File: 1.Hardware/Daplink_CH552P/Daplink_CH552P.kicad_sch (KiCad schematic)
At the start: 19 parts, among them J1 Conn_02x05_Counter_Clockwise, J2 USB_C_Receptacle_USB2.0, SW1 SW_Push, U1 SN74LVC1T45DBV, U2 SN74LVC1T45DBV, U3 CH552G, U4 XC6206P332MR

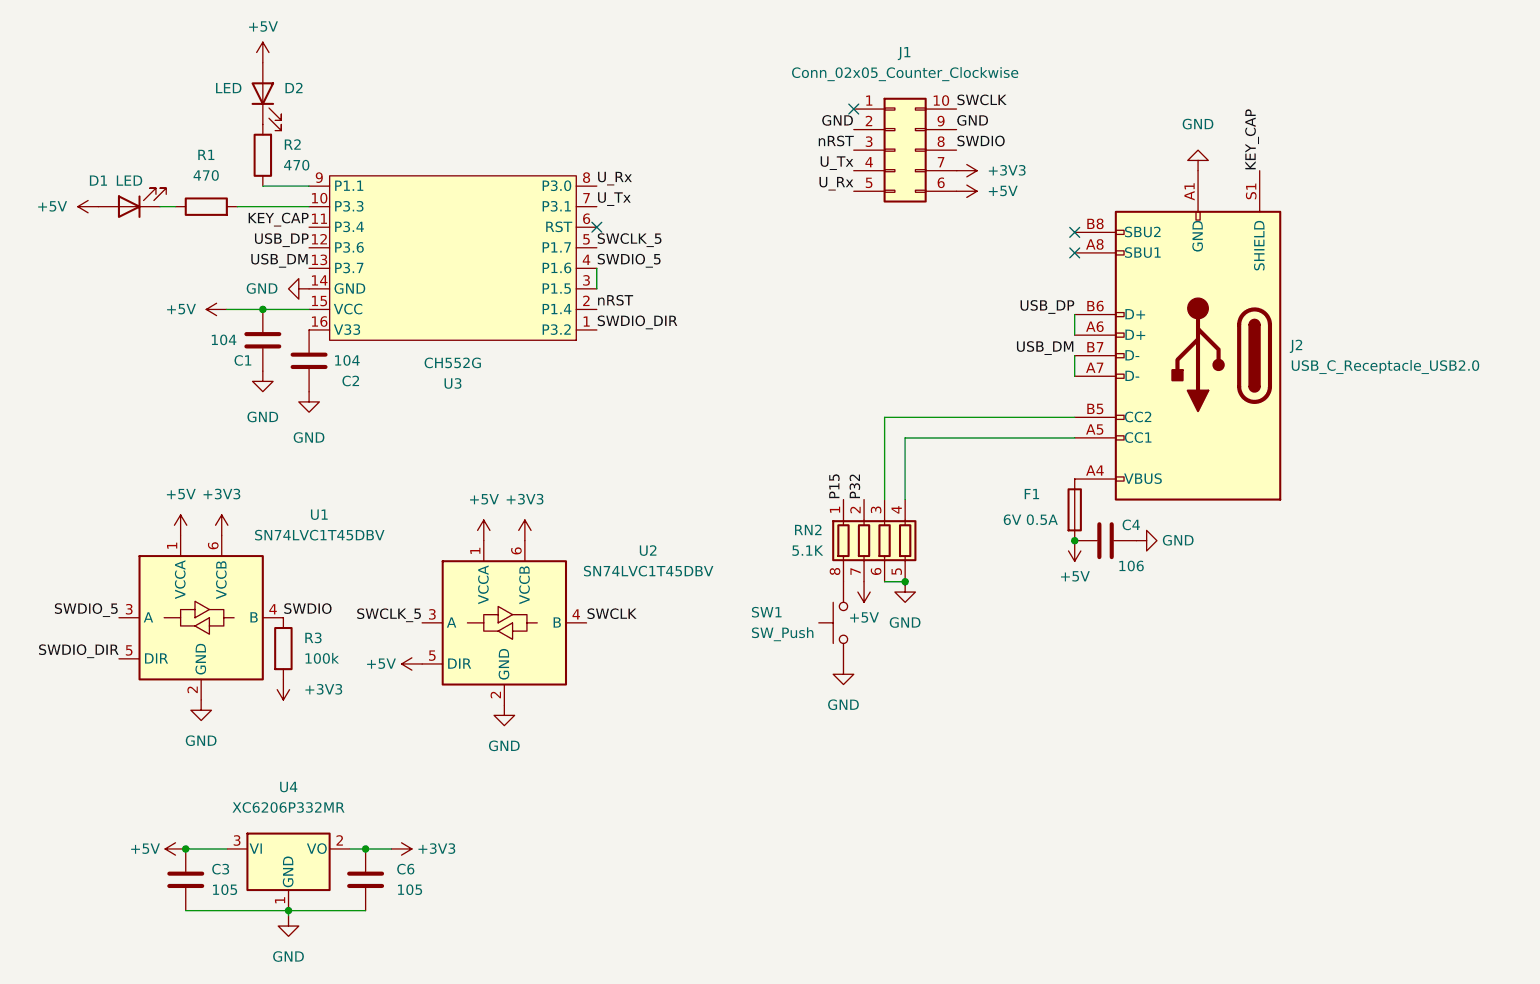
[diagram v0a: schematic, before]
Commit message: 更新调试器硬件（未测试）
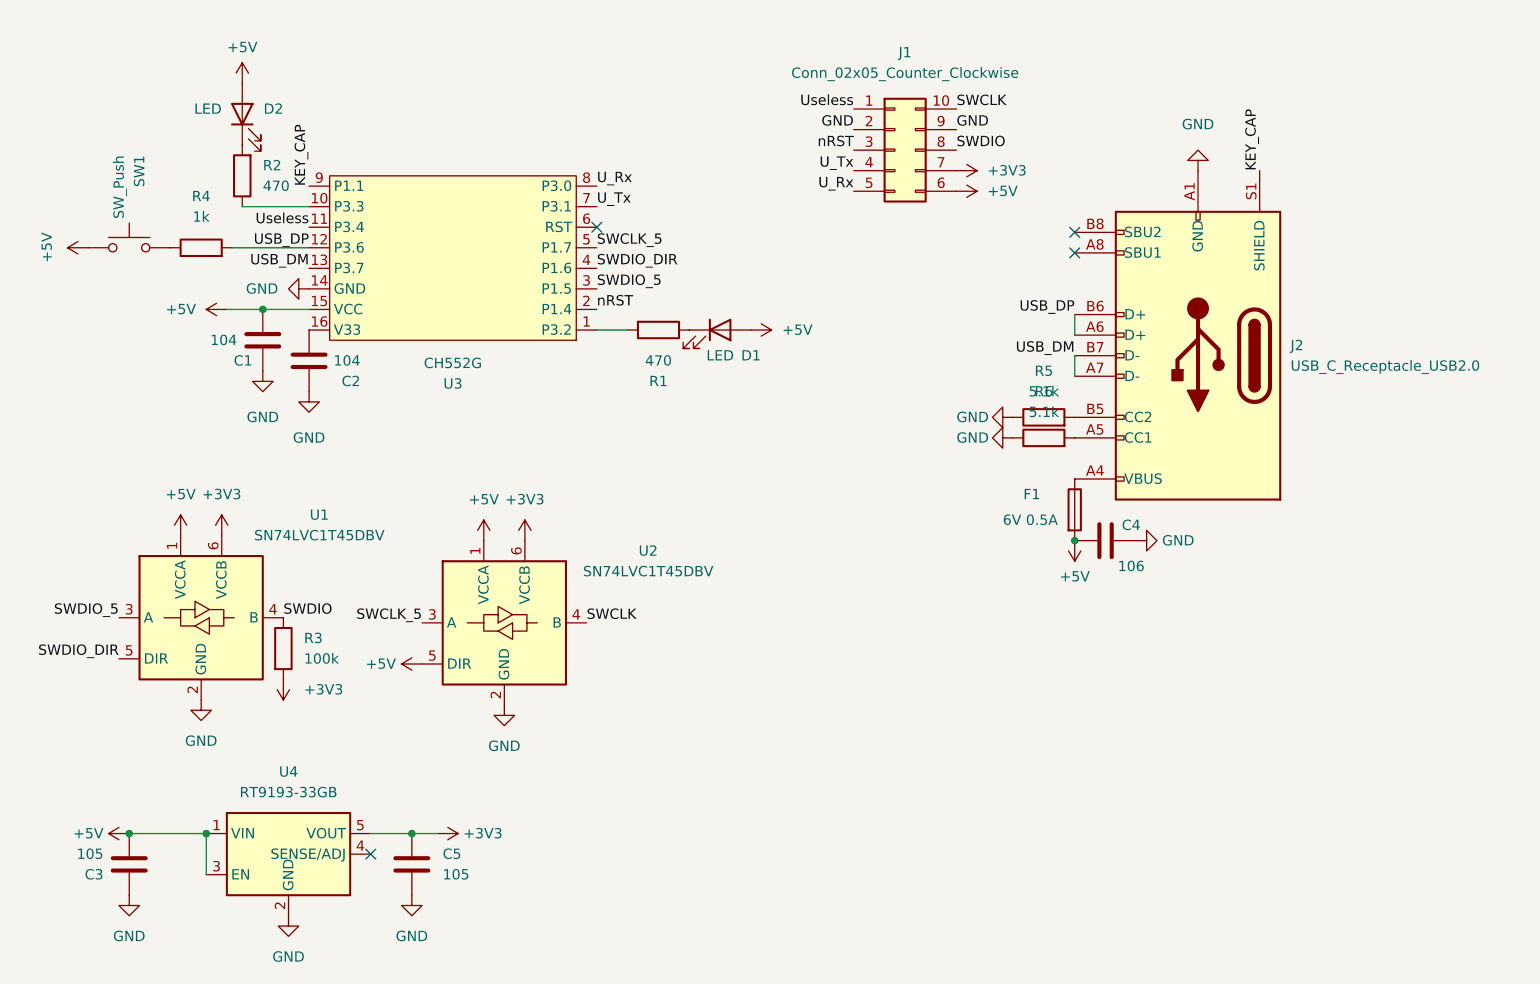
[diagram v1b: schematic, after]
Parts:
- removed C6: 105, Capacitor_SMD:C_0603_1608Metric, symbol Device:C
- removed RN2: 5.1K, Resistor_SMD:R_Array_Concave_4x0603, symbol Device:R_Pack04
- removed U4: XC6206P332MR, Package_TO_SOT_SMD:SOT-23, symbol Regulator_Linear:XC6206PxxxMR
- added C5: 105, Capacitor_SMD:C_0603_1608Metric, symbol Device:C
- added R4: 1k, Resistor_SMD:R_0603_1608Metric, symbol Device:R
- added R5, R6: 5.1k, Resistor_SMD:R_0603_1608Metric, symbol Device:R
- added U4: RT9193-33GB, Package_TO_SOT_SMD:TSOT-23-5, symbol Regulator_Linear:ADP7142AUJZ-5.0
- J1: footprint KiCad库:Connector_2.54mm_2_5P_SMD -> Daplink_Library:Connector_2.54mm_2_5P_SMD
- U3: symbol KiCad库:CH552G -> Daplink_Library:CH552G
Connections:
- net +3V3: now also C5.2, U4.5 (VOUT)
- net +5V: now also C3.1, SW1.1, U4.1 (VIN), U4.3 (EN); no longer C3.2
- net GND: now also C3.2, C5.1, R5.1, R6.1, U4.2 (GND); no longer C3.1, SW1.1
- net KEY_CAP: now also U3.9 (P1.1); no longer U3.11 (P3.4)
- net SWDIO_5: no longer U3.4 (P1.6)
- net SWDIO_DIR: now also U3.4 (P1.6); no longer U3.1 (P3.2)
- net USB_DP: now also R4.2
- net at J2.A5 (CC1): now also R6.2
- net at J2.B5 (CC2): now also R5.2
- net Useless: now reaches J1.1 (Pin_1)
- net Useless: now also U3.11 (P3.4)
- net at U3.10 (P3.3): now also R2.1; no longer R1.2
- net at SW1.2: now also R4.1
- new net: R1.2, U3.1 (P3.2)
